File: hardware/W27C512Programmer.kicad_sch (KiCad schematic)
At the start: 104 parts, among them J1 CTRL, J2 MSB, J3 LSB, J4 Ext_UART, J5 OLED, J6 VP, J7 SAO, Q1 MMBT3904, Q2 MMBT3906, Q3 MMBT3904, Q4 MMBT3904, Q5 MMBT3904, Q6 MMBT3906, Q7 MMBT3906, Q8 MMBT3906, SW1 RST, SW2 USR, U1 MIC2288, U2 74HC573, U3 74HC573, U4 74HC573, U5 28/32 pin ROM

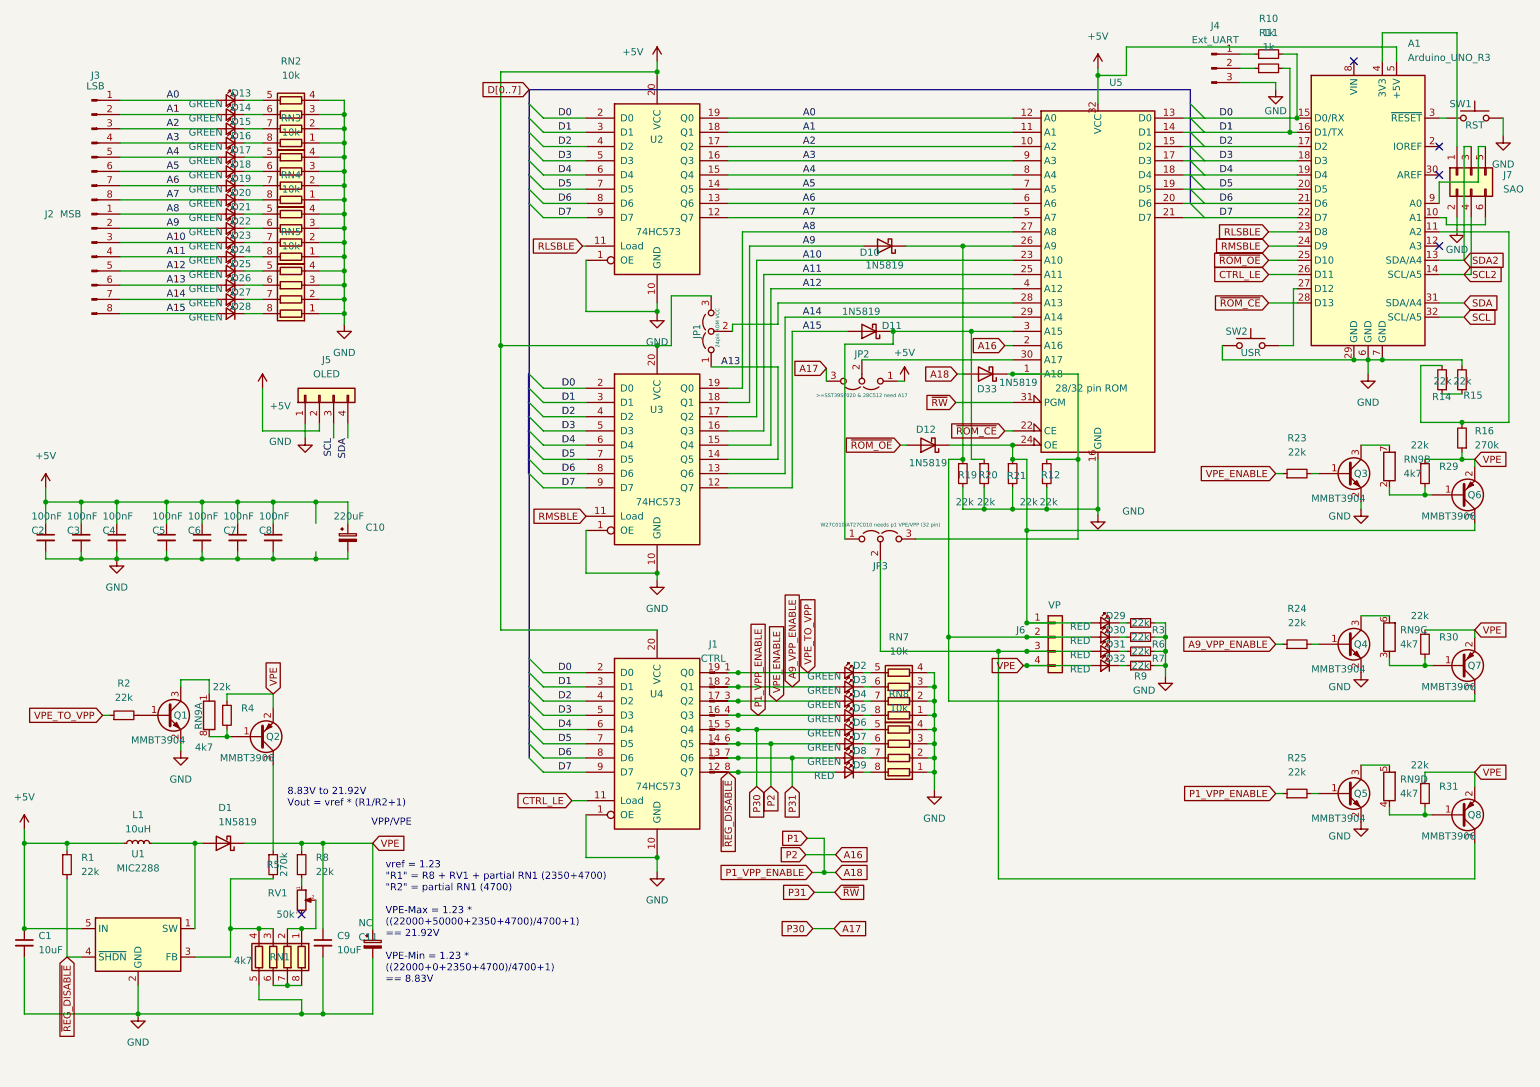
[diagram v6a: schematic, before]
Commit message: Power through address lines
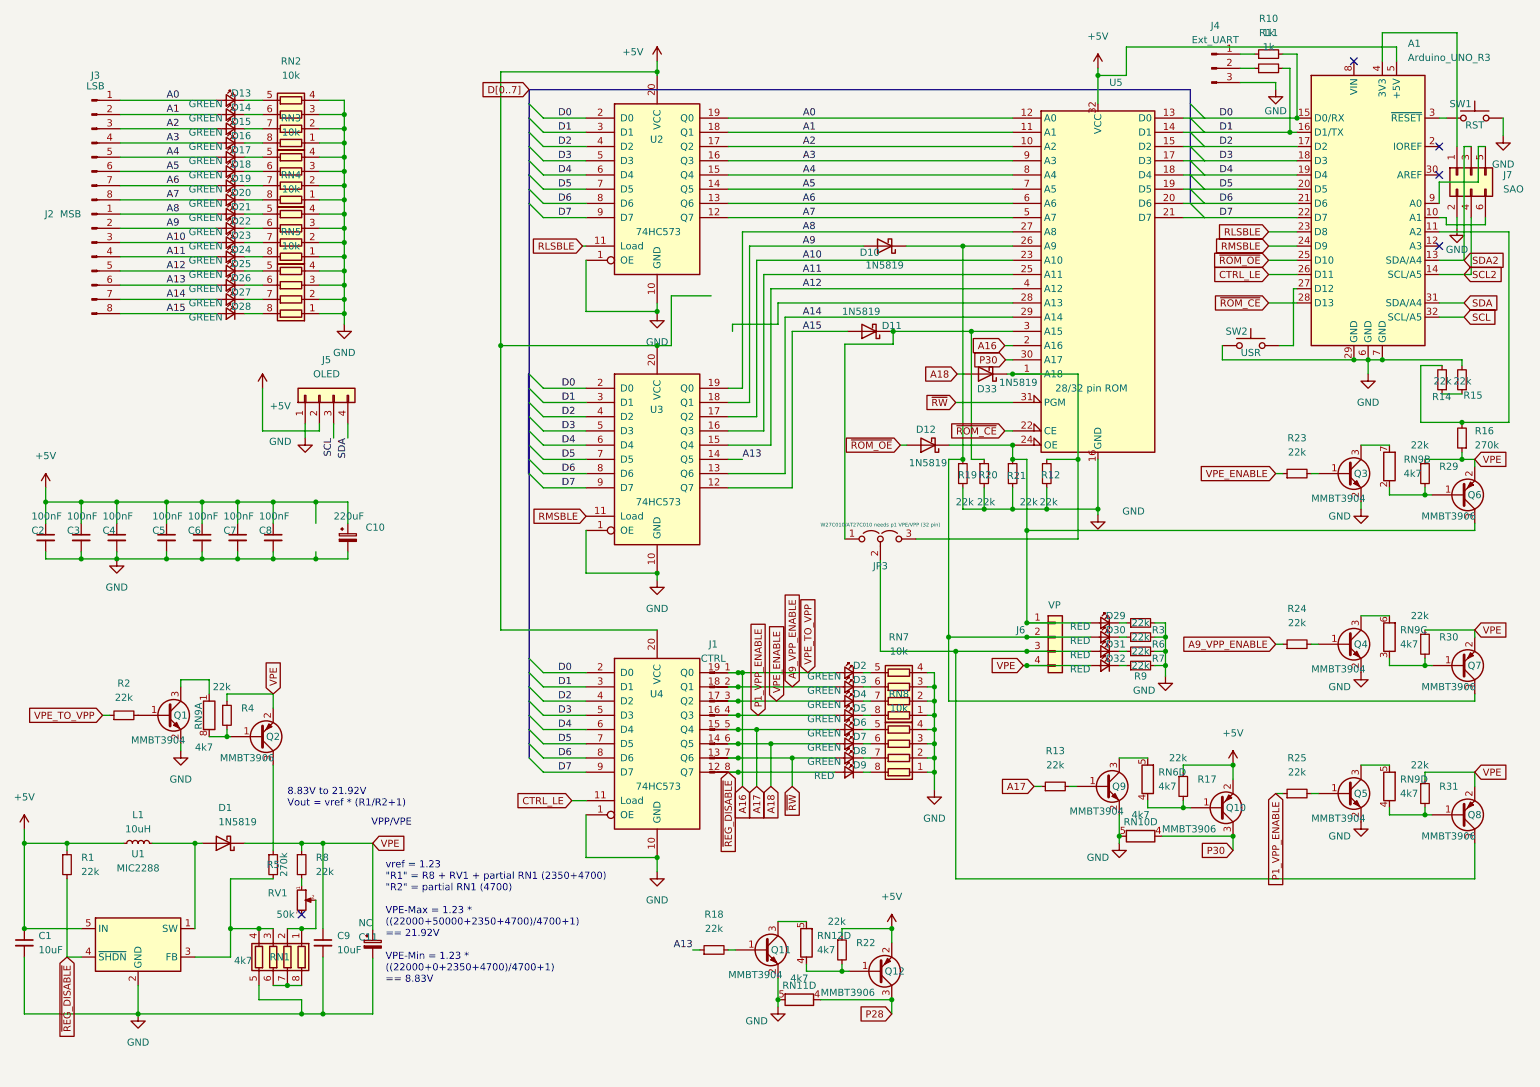
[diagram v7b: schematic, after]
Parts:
- removed JP1: 24pin ROM VCC, Connector_PinHeader_2.54mm:PinHeader_1x03_P2.54mm_Vertical_SolderJumpers, symbol Jumper:Jumper_3_Open
- removed JP2: >=SST39SF020 & 28C512 need A17, Connector_PinHeader_2.54mm:PinHeader_1x03_P2.54mm_Vertical_SolderJumpers, symbol Jumper:Jumper_3_Open
- added Q10, Q12: MMBT3906, Package_TO_SOT_SMD:SOT-23, symbol Transistor_BJT:MMBT3906
- added Q11, Q9: MMBT3904, Package_TO_SOT_SMD:SOT-23, symbol Transistor_BJT:MMBT3904
- added R13, R17, R18, R22: 22k, Resistor_SMD:R_0603_1608Metric, symbol Device:R_Small
- added RN10, RN11, RN12, RN6: 4k7, Resistor_SMD:R_Array_Convex_4x0603, symbol Device:R_Pack04_Split
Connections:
- net VPE_TO_VPP is gone; now on net A16: D2.2 (A), J1.1 (Pin_1), R2.1, U4.19 (Q0)
- net +5V: now also Q10.2 (E), Q12.2 (E), R17.1, R22.1
- net A13: now also R18.1
- net A16: no longer D7.2 (A), J1.6 (Pin_6), U4.14 (Q5)
- net A17: now also R13.1
- net A18: now also D7.2 (A), J1.6 (Pin_6), U4.14 (Q5); no longer D5.2 (A), J1.4 (Pin_4), R25.1, U4.16 (Q3)
- net GND: now also Q11.2 (E), Q9.2 (E), RN10.5 (R4.2), RN11.5 (R4.2)
- net P30: now reaches U5.30 (A17)
- net P30: now also Q10.3 (C), RN10.4 (R4.1)
- net P31 renamed ~{RW}
- new net: Q12.1 (B), R22.2, RN12.4 (R4.1)
- new net: Q11.3 (C), RN12.5 (R4.2)
- new net: Q9.1 (B), R13.2
- new net: Q10.1 (B), R17.2, RN6.4 (R4.1)
- new net: Q9.3 (C), RN6.5 (R4.2)
- new net: Q11.1 (B), R18.2
- new net P1_VPP_ENABLE: D5.2 (A), J1.4 (Pin_4), R25.1, U4.16 (Q3)
- new net P28: Q12.3 (C), RN11.4 (R4.1)

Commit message: Rev2
Hopefully this does what it's supposed to...
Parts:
- removed JP3: W27C010/AT27C010 needs p1 VPE/VPP (32 pin), Jumper:SolderJumper-3_P1.3mm_Open_RoundedPad1.0x1.5mm, symbol Jumper:Jumper_3_Open
- removed RN1: 4k7, Resistor_SMD:R_Array_Convex_4x0603, symbol Device:R_Pack04
- removed RN10, RN11, RN12, RN6, RN9: 4k7, Resistor_SMD:R_Array_Convex_4x0603, symbol Device:R_Pack04_Split
- added C12: 100nF, Capacitor_SMD:C_0603_1608Metric, symbol Device:C_Small
- added J8: Conn_01x02, Connector_PinHeader_2.54mm:PinHeader_1x02_P2.54mm_Vertical, symbol Connector_Generic:Conn_01x02
- added JP4: P1_VPP_JMP, Connector_PinHeader_2.54mm:PinHeader_1x02_P2.54mm_Vertical, symbol Jumper:Jumper_2_Open
- added JP5: A19_CUT, Jumper:SolderJumper-2_P1.3mm_Bridged_RoundedPad1.0x1.5mm, symbol Jumper:SolderJumper_2_Bridged
- added R26, R27, R28, R32, R33, R34, R35, R36, R37, R38, R39, R40, R41: 4k7, Resistor_SMD:R_0402_1005Metric, symbol Device:R_Small
- R13, R17, R18, R22: value 22k -> 4k7; footprint Resistor_SMD:R_0603_1608Metric -> Resistor_SMD:R_0402_1005Metric; LCSC (none) -> C25900
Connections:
- net +5V: now also R13.1, C12.1, J8.1 (Pin_1), R32.1; no longer R17.1, R22.1
- net A13: now also R26.1; no longer R18.1
- net A16: now also D7.2 (A), J1.6 (Pin_6), U4.14 (Q5); no longer D2.2 (A), J1.1 (Pin_1), R2.1, U4.19 (Q0)
- net A17: now also R22.1; no longer R13.1
- net GND: now also R18.1, C12.2, J8.2 (Pin_2), R27.1, R37.2, R41.2
- net P1_VPP_ENABLE: now also D33.2 (A)
- net P28: now also U5.28 (A13), R27.2
- net P30: now also R18.2
- net at D11.1 (K), R20.1, U5.3 (A15): now also JP4.2 (B)
- net at D31.2 (A), J6.3 (Pin_3), Q8.3 (C): now also JP5.1 (A)
- net at Q1.3 (C): now also R34.1
- net at Q2.1 (B), R4.2: now also R34.2
- net at R5.2, U1.3 (FB): now also R36.1, R37.1
- net at Q7.1 (B), R30.2: now also R39.2
- net at Q12.1 (B): now also R28.2, R32.2; no longer R22.2
- net at Q11.3 (C): now also R28.1
- net at Q4.3 (C): now also R39.1
- net at Q8.1 (B), R31.2: now also R38.2
- net at Q5.3 (C): now also R38.1
- net at Q6.1 (B), R29.2: now also R40.2
- net at Q3.3 (C): now also R40.1
- net at R13.2: now also Q10.1 (B), R17.2; no longer Q9.1 (B)
- net at Q9.3 (C): now also R17.1
- net at RV1.2: now also R33.1, R35.1
- net at Q11.1 (B): now also R26.2; no longer R18.2
- net at D33.1 (K), R12.1, U5.1 (A18): now also JP4.1 (A), JP5.2 (B)
- net at A1.12 (A3): now also R41.1
- removed net A18: D33.2 (A), D7.2 (A), J1.6 (Pin_6), U4.14 (Q5)
- net ~{RW} renamed P31
- new net: R33.2, R35.2, R36.2
- new net: Q9.1 (B), R22.2
- new net VPE_TO_VPP: D2.2 (A), J1.1 (Pin_1), R2.1, U4.19 (Q0)
- no-connect marks 5 -> 4
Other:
- moved on the sheet: D33, J5
